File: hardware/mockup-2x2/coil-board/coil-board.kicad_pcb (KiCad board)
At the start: 4 copper layers, 100 x 100 mm, 9 parts, among them J1 COIL_JOINT_1x10, M1 NPTH, M2 NPTH, M3 NPTH, M4 NPTH

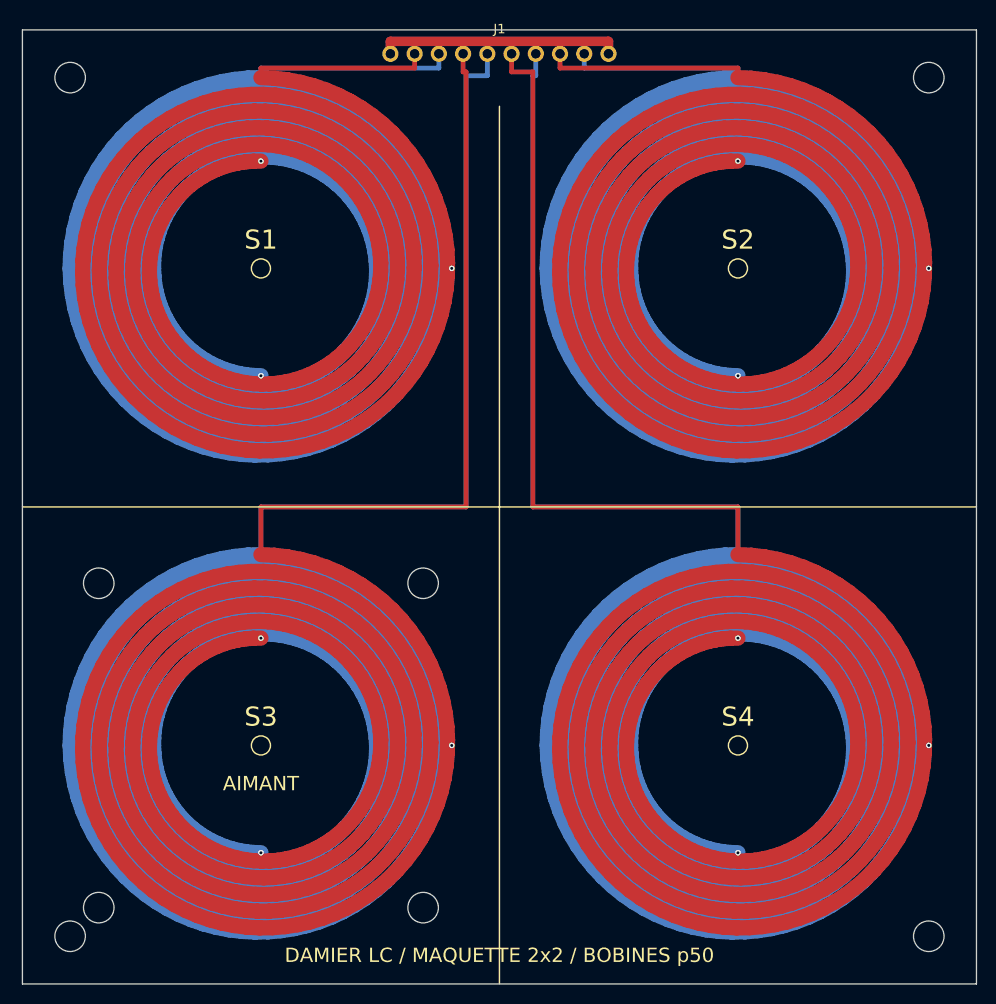
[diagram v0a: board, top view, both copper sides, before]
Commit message: Carte bobines : 8 LED WS2812B chainees aux coins des cases
Deux LED RGB adressables par case aux coins opposes (diagonale NE-SO
pour la case 2, son coin NO tombant sous la rangee du connecteur),
chacune avec 100 nF et sa paire de vias choisie par degagement.
Distribution : donnees chainees sur In1 dans les couloirs, boucle 5V
sur In2 (esquives des empilements de terminaux et de la rangee de
pads), masse en face arriere (boucle, epine centrale, eperons choisis
par un petit solveur garde : droit, en L, ou secours In1 avec via).
Connecteur commun porte a 12 broches (donnees et 5V en bout), lane
d'echappee de la case 4 decalee pour les pads recentres. Garde
geometrique au build contre spirales, terminaux, barillets et bord ;
test d'ecart echantillonne etendu au sous-systeme LED, 9 tests verts.
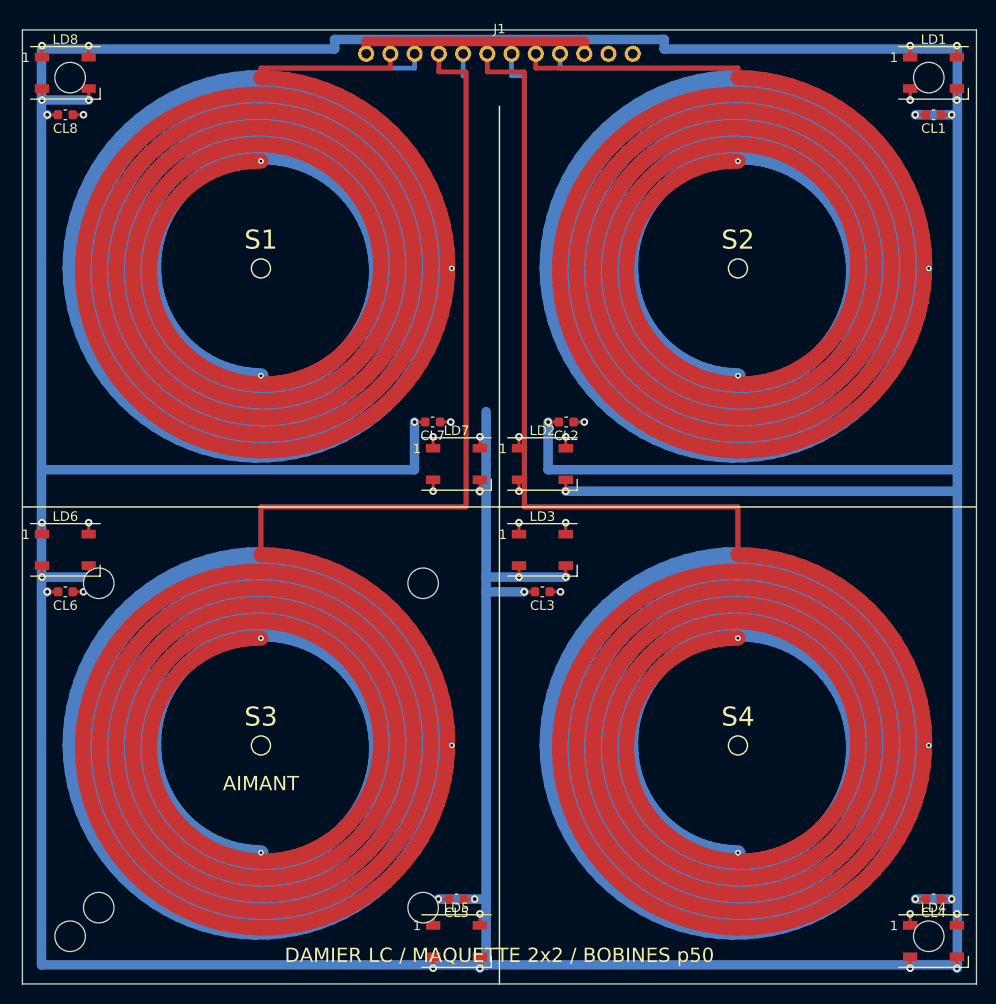
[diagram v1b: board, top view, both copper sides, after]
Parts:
- added CL1: 100n, Capacitor_SMD:C_0603_1608Metric, F.Cu at (95.5, 8.90)
- added CL2: 100n, Capacitor_SMD:C_0603_1608Metric, F.Cu at (57.0, 41.1)
- added CL3: 100n, Capacitor_SMD:C_0603_1608Metric, F.Cu at (54.5, 58.9)
- added CL4: 100n, Capacitor_SMD:C_0603_1608Metric, F.Cu at (95.5, 91.1)
- added CL5: 100n, Capacitor_SMD:C_0603_1608Metric, F.Cu at (45.5, 91.1)
- added CL6: 100n, Capacitor_SMD:C_0603_1608Metric, F.Cu at (4.50, 58.9)
- added CL7: 100n, Capacitor_SMD:C_0603_1608Metric, F.Cu at (43.0, 41.1)
- added CL8: 100n, Capacitor_SMD:C_0603_1608Metric, F.Cu at (4.50, 8.90)
- added LD1: WS2812B, LED_SMD:LED_WS2812B_PLCC4_5.0x5.0mm_P3.2mm, F.Cu at (95.5, 4.50)
- added LD2: WS2812B, LED_SMD:LED_WS2812B_PLCC4_5.0x5.0mm_P3.2mm, F.Cu at (54.5, 45.5)
- added LD3: WS2812B, LED_SMD:LED_WS2812B_PLCC4_5.0x5.0mm_P3.2mm, F.Cu at (54.5, 54.5)
- added LD4: WS2812B, LED_SMD:LED_WS2812B_PLCC4_5.0x5.0mm_P3.2mm, F.Cu at (95.5, 95.5)
- added LD5: WS2812B, LED_SMD:LED_WS2812B_PLCC4_5.0x5.0mm_P3.2mm, F.Cu at (45.5, 95.5)
- added LD6: WS2812B, LED_SMD:LED_WS2812B_PLCC4_5.0x5.0mm_P3.2mm, F.Cu at (4.50, 54.5)
- added LD7: WS2812B, LED_SMD:LED_WS2812B_PLCC4_5.0x5.0mm_P3.2mm, F.Cu at (45.5, 45.5)
- added LD8: WS2812B, LED_SMD:LED_WS2812B_PLCC4_5.0x5.0mm_P3.2mm, F.Cu at (4.50, 4.50)
- J1: value COIL_JOINT_1x10 -> COIL_JOINT_1x12; footprint coilgen:COIL_JOINT_1x10 -> coilgen:COIL_JOINT_1x12
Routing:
- net LED_5V: track 0.00 -> 641.5 mm, vias 0 -> 16
- net GND: track 25.5 -> 659.5 mm, vias 0 -> 16
- net LED_L7: track 0.00 -> 99.8 mm, vias 0 -> 2
- net LED_L5: track 0.00 -> 93.7 mm, vias 0 -> 2
- net LED_L3: track 0.00 -> 91.1 mm, vias 0 -> 2
- net LED_L1: track 0.00 -> 87.4 mm, vias 0 -> 2
- net LED_L6: track 0.00 -> 65.3 mm, vias 0 -> 2
- net LED_L4: track 0.00 -> 53.3 mm, vias 0 -> 2
- net LED_DIN: track 0.00 -> 42.8 mm, vias 0 -> 1
- net LED_L2: track 0.00 -> 10.6 mm, vias 0 -> 2
- net C2: track 2101.3 -> 2106.4 mm
- net C1: track 2101.3 -> 2096.3 mm
- net C4: track 2212.1 -> 2216.6 mm
- net LED_END: track 0.00 -> 1.20 mm, vias 0 -> 1
- net C3: track 2212.1 -> 2212.7 mm
